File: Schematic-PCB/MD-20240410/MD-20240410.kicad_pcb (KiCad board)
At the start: 2 copper layers, 100.5 x 56.4 mm, 49 parts, among them J1 Conn_01x05_Pin, J2 Conn_01x04_Pin, J3 Conn_01x02_Pin, J4 Conn_01x02_Pin, J5 Conn_01x02_Pin, J6 Conn_01x02_Pin, J7 Conn_01x02_Pin, J8 Conn_01x15_Pin, Q3 NMOS, Q4 NMOS

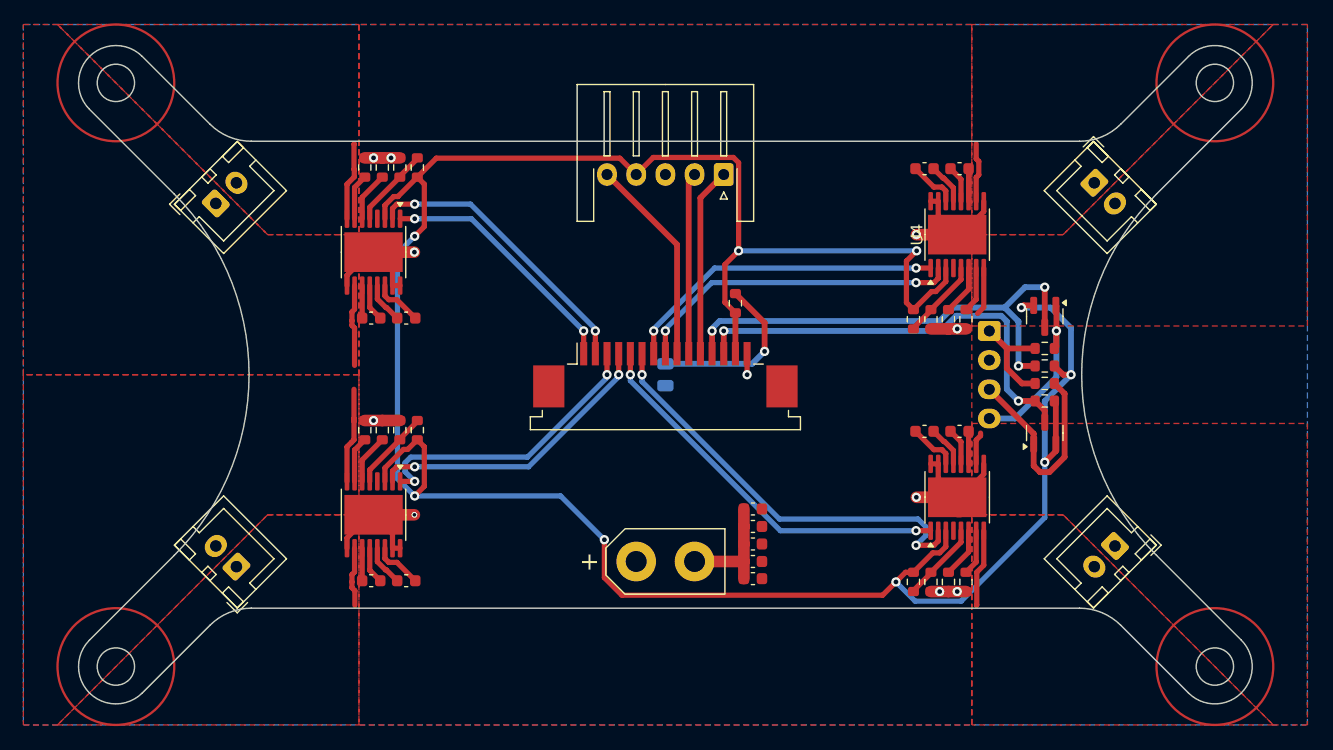
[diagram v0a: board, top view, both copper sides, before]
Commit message: MD基板のPCBを修正し製造用ファイルを出力した
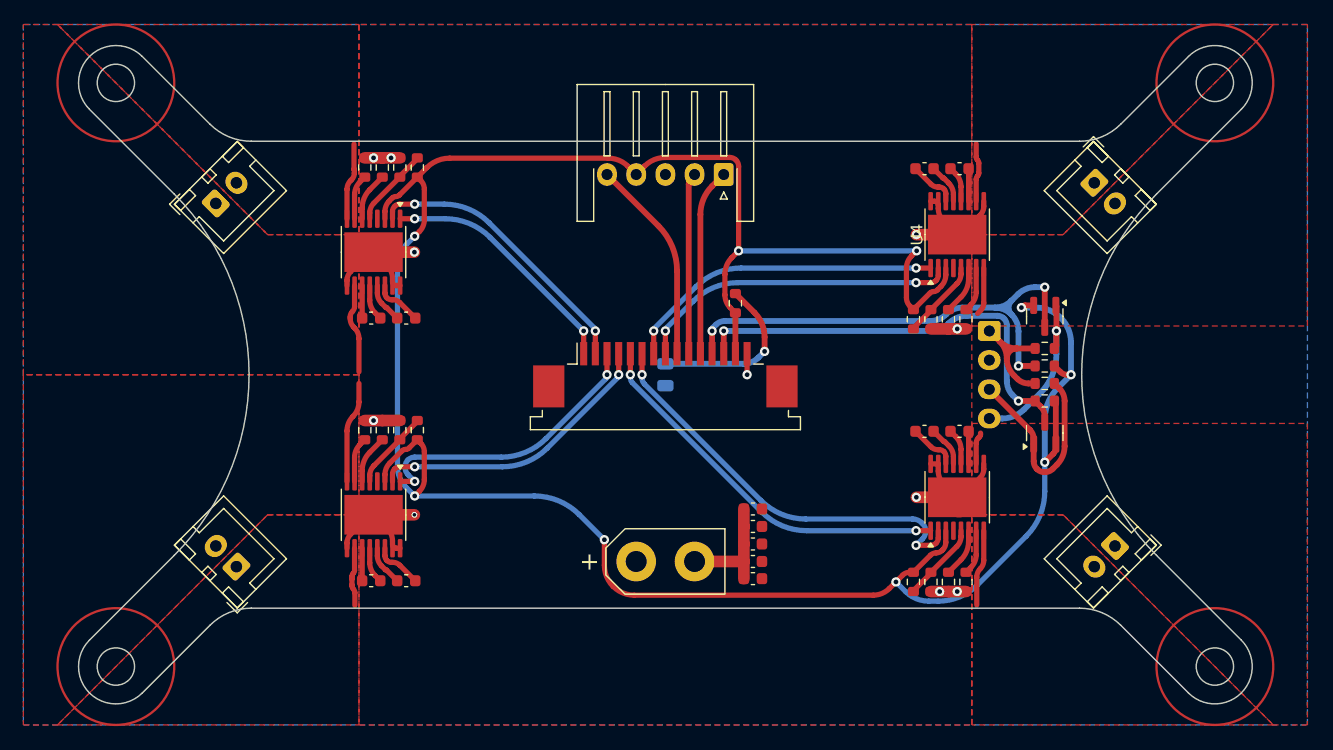
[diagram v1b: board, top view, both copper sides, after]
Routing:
- net SLEEP-1: track 218.3 -> 214.0 mm
- net +5V: track 9.21 -> 11.0 mm
- net Line-MD-Main=RX_3.3V: track 42.5 -> 44.0 mm
- net GND: track 70.6 -> 69.2 mm
- net OUT2-1: track 7.02 -> 7.68 mm
- net OUT1-2: track 8.14 -> 8.64 mm

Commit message: MD基板の発注用ファイルを作成した
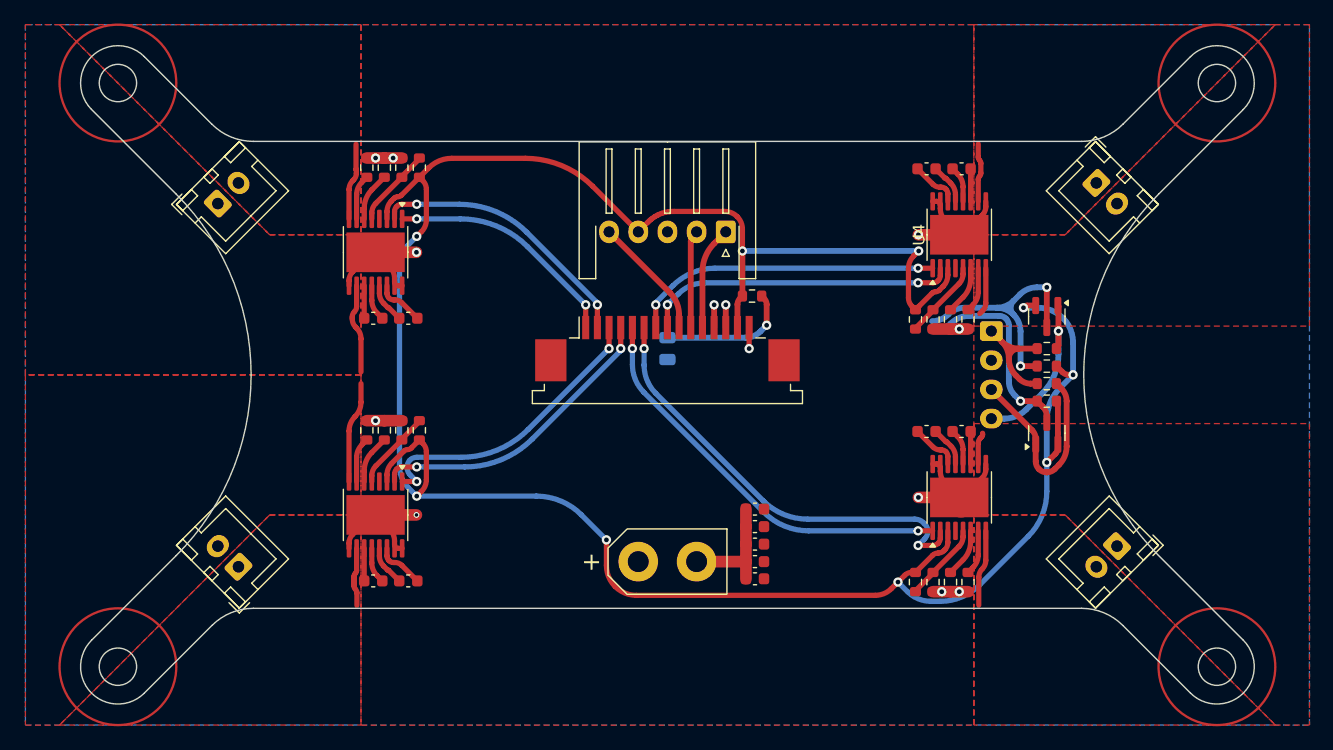
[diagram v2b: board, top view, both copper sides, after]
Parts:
- moved J1 4.92 mm to (5.17, -12.2)
- moved D1 2.24 mm to (0.17, -2.24)
- moved J8 2.24 mm to (0.17, -2.24)
- moved R1 1.55 mm to (7.42, -6.74), turned to 0 degrees
- moved C10 0.18 mm to (-25.0, 17.7)
- moved C9 0.18 mm to (-22.0, 17.7)
- moved C11 0.18 mm to (22.4, 4.86)
- moved C12 0.18 mm to (25.4, 4.86)
- moved J2 0.18 mm to (27.9, -3.74)
- moved R10 0.18 mm to (-22.6, 4.76)
- moved R11 0.18 mm to (-25.6, 4.76)
- moved R16 0.18 mm to (24.4, -4.74)
- moved R17 0.18 mm to (21.4, -4.74)
- moved R18 0.18 mm to (22.9, -4.74)
- moved R19 0.18 mm to (25.9, -4.74)
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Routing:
- net Line-MD-Main=RX_3.3V: track 44.0 -> 25.0 mm
- net Line-MD-Main=TX_3.3V: track 37.3 -> 19.6 mm
- net ball02k: track 16.0 -> 8.86 mm
- net KickerSignal-main: track 15.5 -> 8.37 mm
- net ball01k: track 17.6 -> 10.6 mm
- net SLEEP-1: track 214.0 -> 208.7 mm
- net Net-(D1-A): track 14.7 -> 11.5 mm
- net PH-3: track 36.2 -> 38.5 mm
- net EN-3: track 33.1 -> 35.2 mm
- net EN-1: track 21.4 -> 20.3 mm
- net PH-2: track 25.2 -> 26.3 mm
- net PH-1: track 24.6 -> 23.8 mm
- net EN-2: track 25.2 -> 25.9 mm
- net EN-4: track 27.7 -> 27.1 mm
- net PH-4: track 27.8 -> 27.2 mm

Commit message: MD基板を完成させた
DRだけお願い
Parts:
- moved Q3 25.0 mm to (15.2, 12.9), turned to 90 degrees
- moved Q4 22.6 mm to (11.5, 12.9)
- moved R20 18.9 mm to (20.0, 13.2), turned to -90 degrees
- moved R22 18.1 mm to (18.2, 13.2), turned to -90 degrees
- moved R21 17.3 mm to (16.5, 4.00), turned to -90 degrees
- moved R23 16.2 mm to (16.5, 1.00), turned to -90 degrees
- moved J2 13.7 mm to (14.2, -3.75)
- moved D1 0.27 mm to (0.00, -2.04)
- moved J8 0.27 mm to (0.00, -2.04)
- moved C1 0.06 mm to (-22.0, -4.78)
- moved C10 0.06 mm to (-25.0, 17.7)
- moved C11 0.06 mm to (22.4, 4.92)
- moved C12 0.06 mm to (25.4, 4.92)
- moved C13 0.06 mm to (22.4, -17.6)
- moved C14 0.06 mm to (25.4, -17.6)
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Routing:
- net SLEEP-1: track 208.7 -> 175.2 mm, vias 9 -> 5
- net Line-MD-Main=TX_3.3V: track 19.6 -> 32.1 mm, vias 2 -> 3
- net Line-MD-Main=RX_3.3V: track 25.0 -> 33.7 mm
- net PH-2: track 26.3 -> 30.0 mm
- net Line-MD-Main=TX_5V: track 18.2 -> 21.7 mm, vias 0 -> 2
- net EN-2: track 25.9 -> 29.3 mm
- net EN-3: track 35.2 -> 38.0 mm
- net PH-3: track 38.5 -> 40.5 mm
- net +5V: track 11.0 -> 9.61 mm
- net Line-MD-Main=RX_5V: track 14.6 -> 13.3 mm
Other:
- board text added: "1"
- board text added: "15"
- board text added: "KICKER"
- board text added: "LOGIC PWR"
- board text added: "MD-Board #001"

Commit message: MDのDRしたよ
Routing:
- net SLEEP-1: track 175.2 -> 175.8 mm

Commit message: MD基板の再DRが完了した
製造用ファイル出力済み
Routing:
- net SLEEP-1: track 175.8 -> 177.8 mm

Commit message: MD基板 電源用XTコネクタ フットプリント修正済み
ごめんなさい
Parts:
- moved C10 0.19 mm to (-25.2, 17.6)
- moved C9 0.19 mm to (-22.2, 17.6)
- moved R10 0.19 mm to (-22.8, 4.75)
- moved R11 0.19 mm to (-25.8, 4.75)
- moved R16 0.19 mm to (24.2, -4.75)
- moved R17 0.19 mm to (21.2, -4.75)
- moved R18 0.19 mm to (22.7, -4.75)
- moved R19 0.19 mm to (25.7, -4.75)
- moved R8 0.19 mm to (-24.3, 4.75)
- moved R9 0.19 mm to (-21.3, 4.75)
- moved C1 0.19 mm to (-22.2, -4.85)
- moved C2 0.19 mm to (-25.2, -4.85)
- moved R12 0.19 mm to (24.2, 17.8)
- moved R13 0.19 mm to (21.2, 17.8)
- moved R14 0.19 mm to (22.7, 17.8)
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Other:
- board text added: "MD-Board #002"
- board text removed: "MD-Board #001"

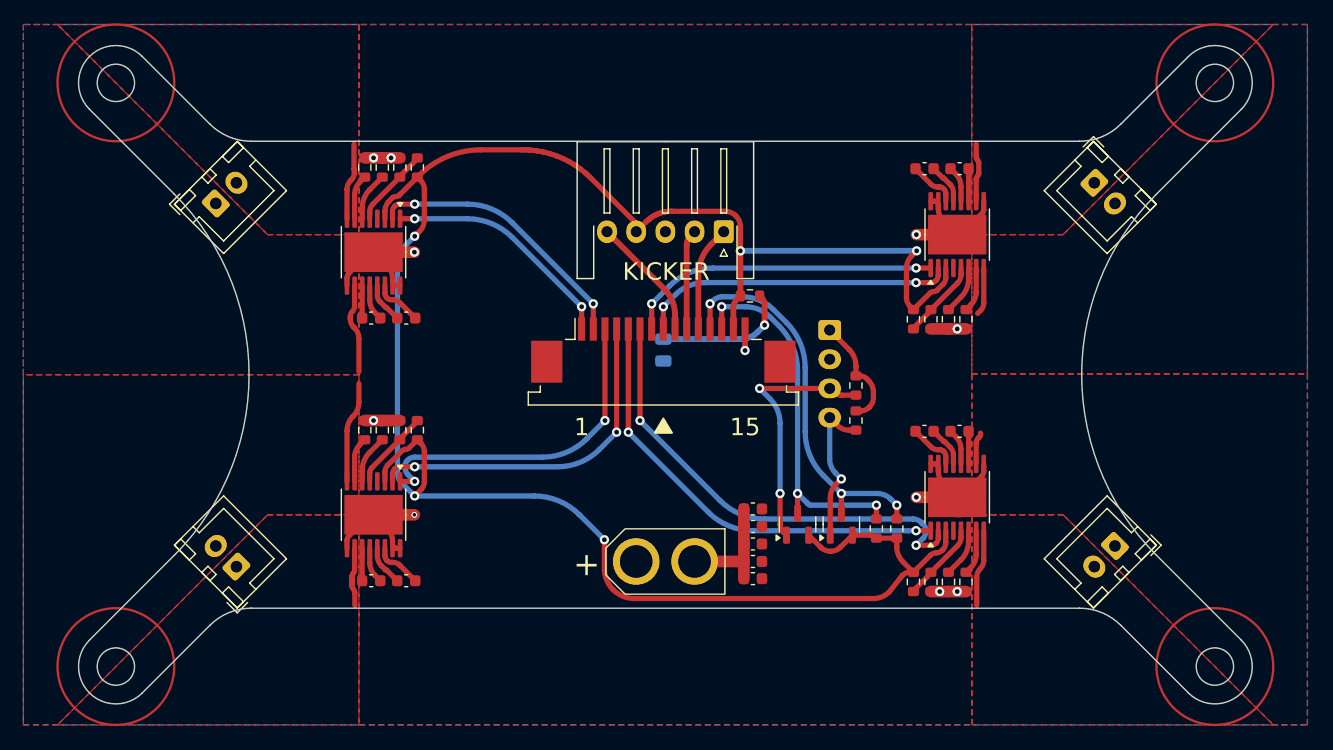
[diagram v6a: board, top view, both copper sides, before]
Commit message: MD基板とキッカー基板を編集した
接続方法をピンヘッダ&ピンソケットに変更してみた
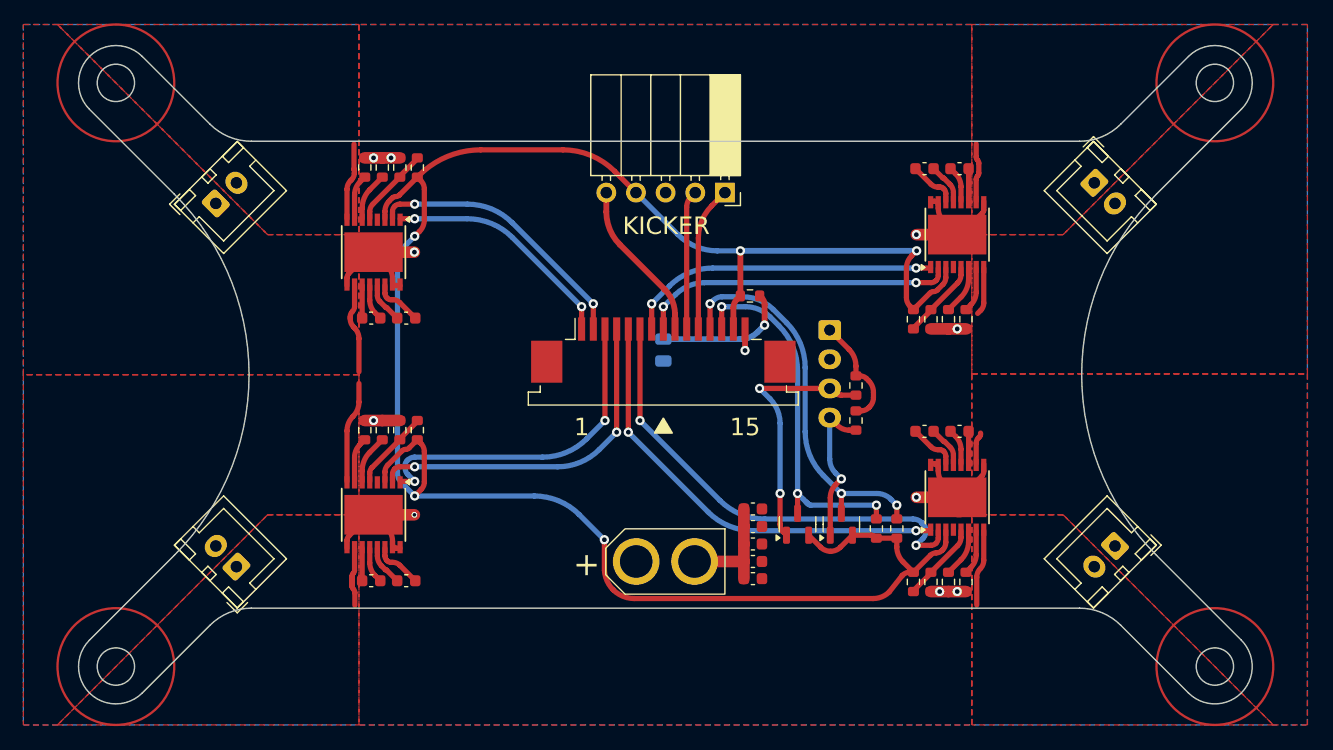
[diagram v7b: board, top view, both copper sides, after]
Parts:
- D1: value LED -> PWR
- J1: footprint Connector_JST:JST_XH_S5B-XH-A-1_1x05_P2.50mm_Horizontal -> Connector_PinSocket_2.54mm:PinSocket_1x05_P2.54mm_Horizontal
- U1, U2, U3, U4: footprint Package_SO:HTSSOP-16-1EP_4.4x5mm_P0.65mm_EP3.4x5mm_Mask2.46x2.31mm -> Package_SO:HTSSOP-16-1EP_4.4x5mm_P0.65mm_EP3.4x5mm
- moved J1 3.35 mm to (5.10, -15.6), turned to -90 degrees
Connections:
- net VM renamed VCC
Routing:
- net SLEEP-1: track 177.8 -> 173.4 mm
- net ball02k: track 9.06 -> 12.4 mm
- net KickerSignal-main: track 8.56 -> 11.9 mm
- net ball01k: track 10.6 -> 13.8 mm
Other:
- board text added: "+"

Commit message: キッカー基板を更新した
MDとの接続をピンヘッダ/ピンソケットを使う方式に変更した
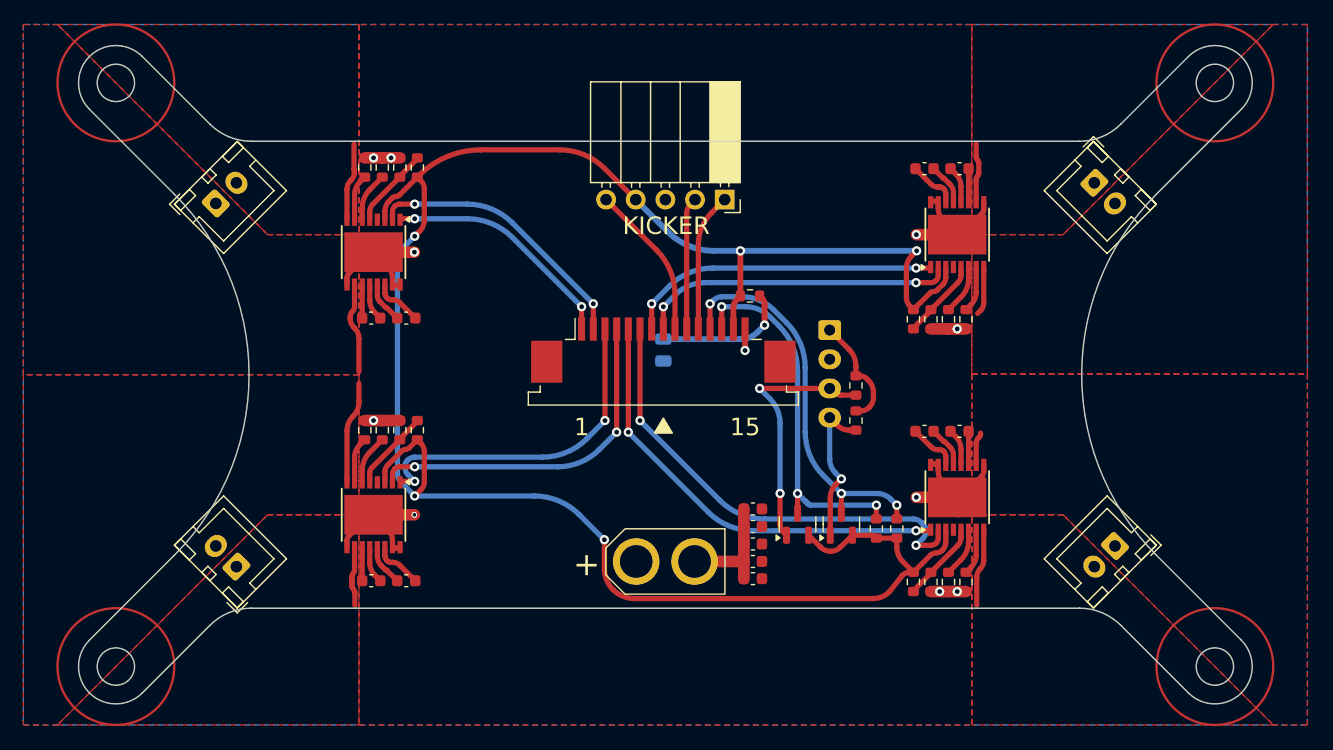
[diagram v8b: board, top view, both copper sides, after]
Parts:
- moved J1 0.60 mm to (5.08, -15.0)
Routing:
- net KickerSignal-main: track 11.9 -> 11.3 mm
- net ball02k: track 12.4 -> 11.8 mm
- net ball01k: track 13.8 -> 13.3 mm
